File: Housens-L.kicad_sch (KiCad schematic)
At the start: 47 parts, among them J1 JTAG/SWD, J2 USB_C_2.0, Q1 BSS138DWQ, SW1 RESET, SW2 USER, U1 MCP1603, U2 BME280, U3 OPT3005, U4 STM32WB55CGUx, U5 STCC4, U6 REG710NA-3.3, Y1 32MHz, Y2 32.768kHz

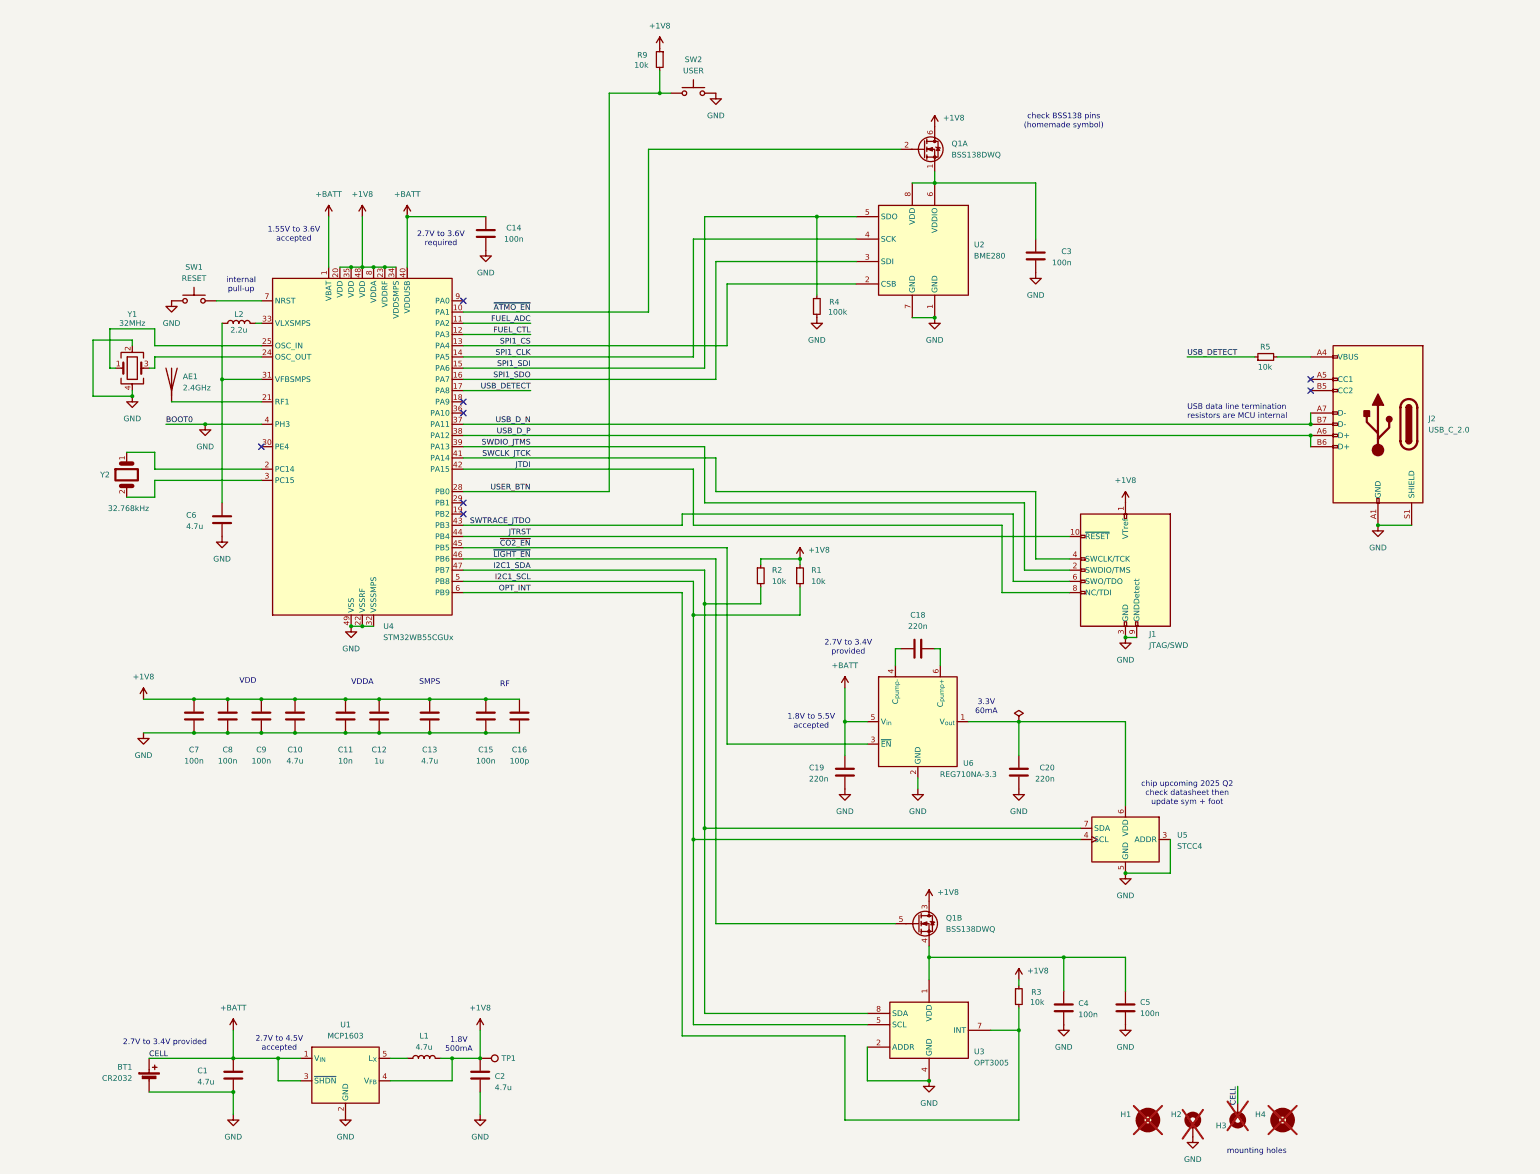
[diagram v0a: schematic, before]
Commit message: Use proper load switch instead of plain FET
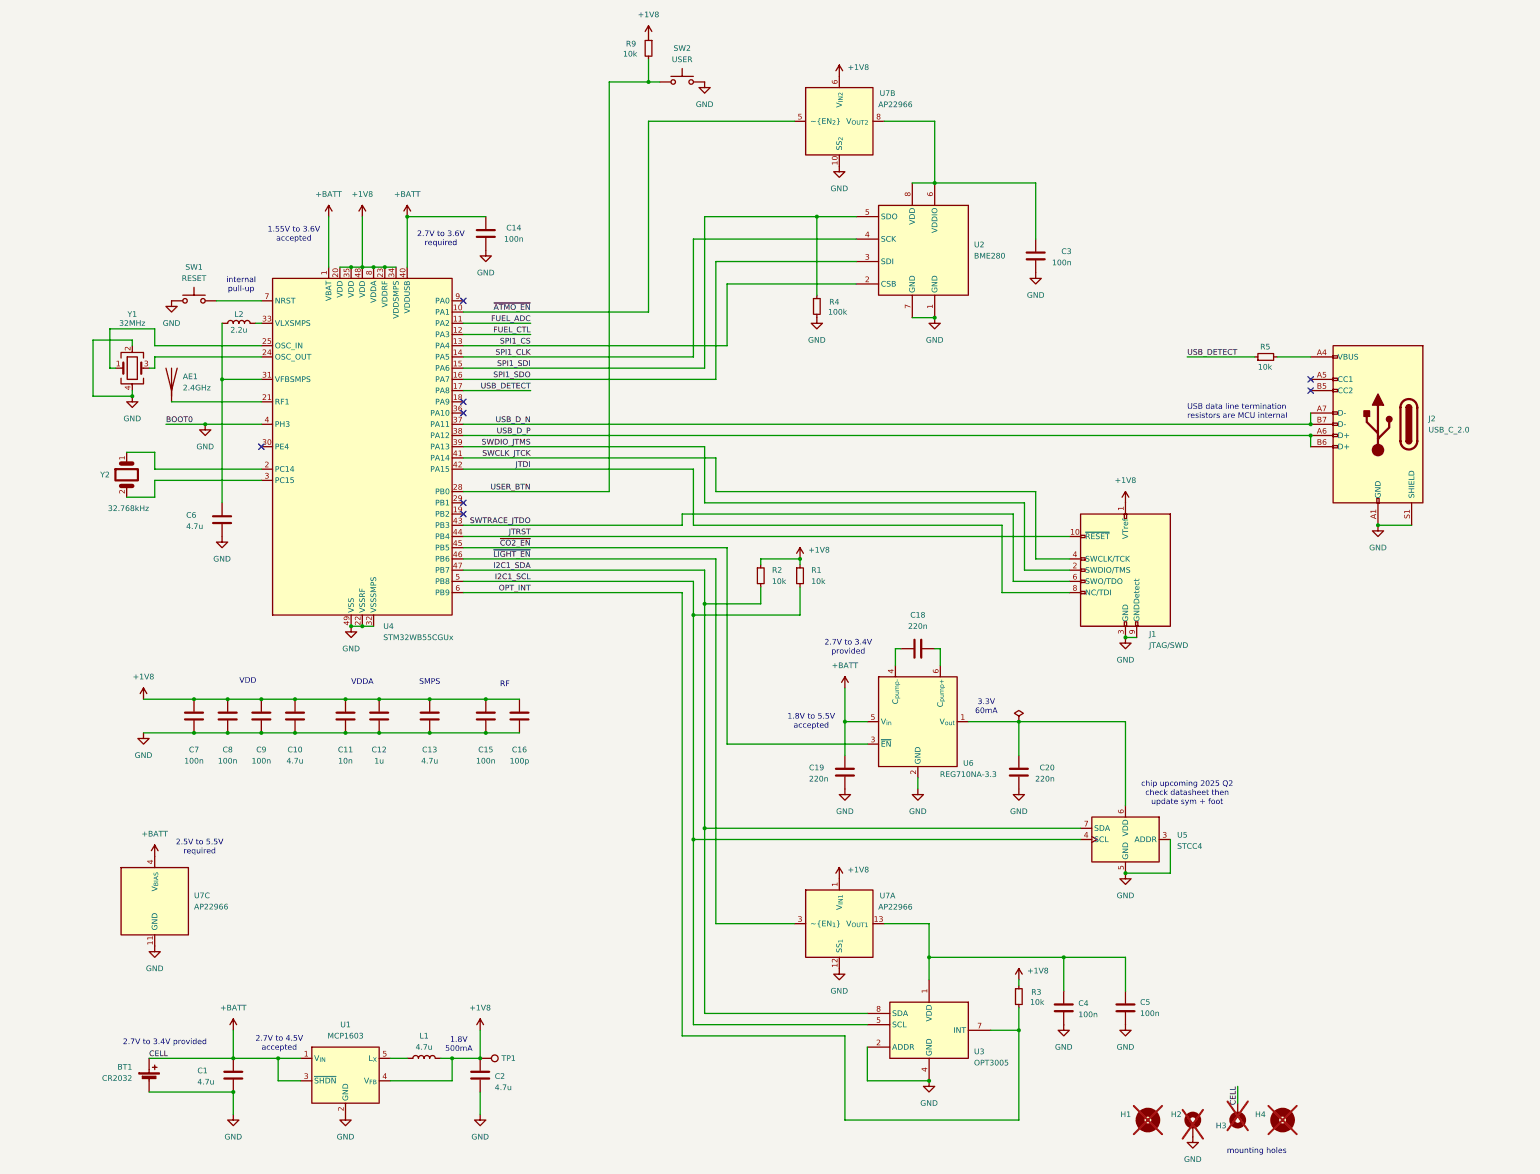
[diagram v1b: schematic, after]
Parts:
- removed Q1: BSS138DWQ, Package_TO_SOT_SMD:SOT-363_SC-70-6, symbol Invented:BSS138DWQ
- added U7: AP22966, Invented:DFN-14-1EP_3x2mm_P0.4mm_EP1.78x1.35mm_AP22966, symbol Invented:AP22966_Split
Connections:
- net +1V8: now also U7.1 (V_{IN1}), U7.2 (V_{IN1}), U7.6 (V_{IN2}), U7.7 (V_{IN2})
- net +BATT: now also U7.4 (V_{BIAS})
- net GND: now also U7.10 (SS_{2}), U7.11 (GND), U7.12 (SS_{1}), U7.15 (GND)
- net ~{ATMO_EN}: now also U7.5 (~{EN_{2}})
- net ~{LIGHT_EN}: now also U7.3 (~{EN_{1}})
- net at C4.1, C5.1, U3.1 (VDD): now also U7.13 (V_{OUT1}), U7.14 (V_{OUT1})
- net at C3.1, U2.6 (VDDIO), U2.8 (VDD): now also U7.8 (V_{OUT2}), U7.9 (V_{OUT2})
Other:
- note added: "2.5V to 5.5V required"
- note removed: "check BSS138 pins (homemade symbol)"
- moved on the sheet: R9, SW2

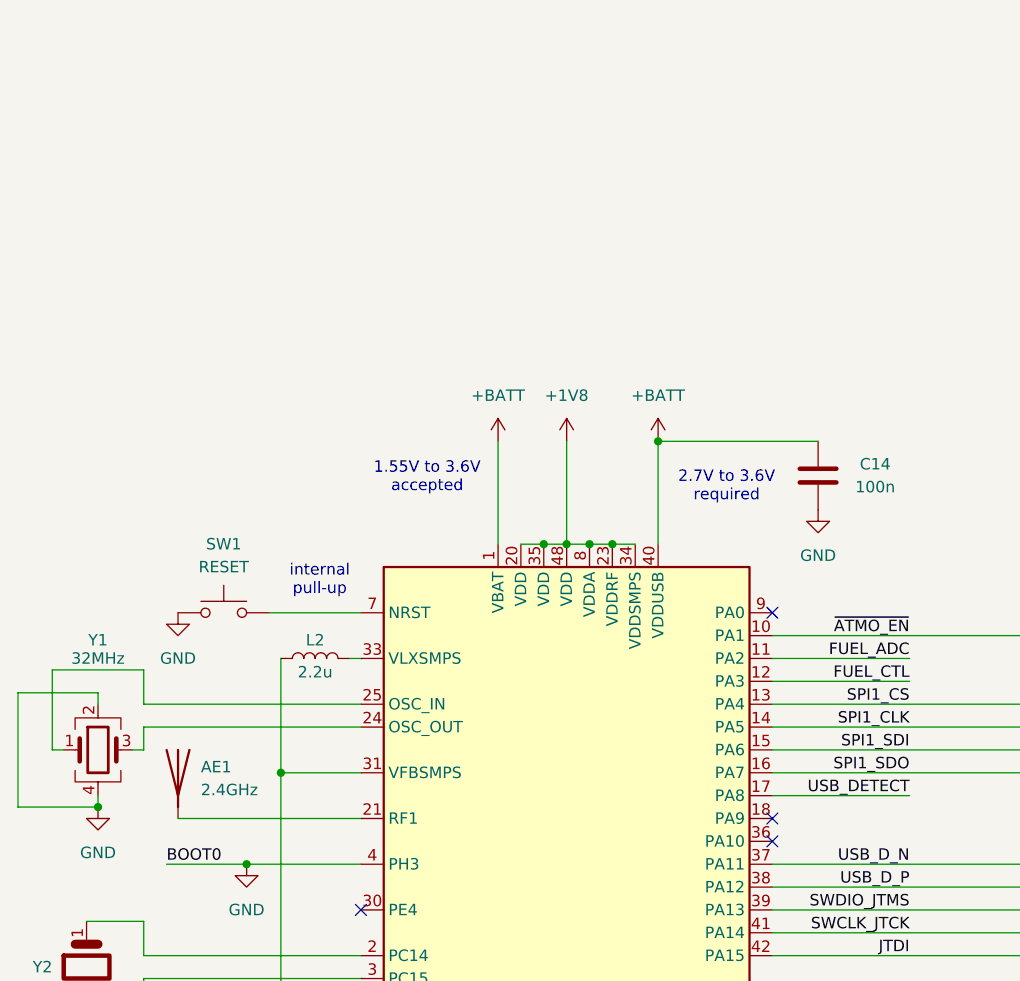
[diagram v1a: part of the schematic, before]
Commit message: Add matching circuit to antenna
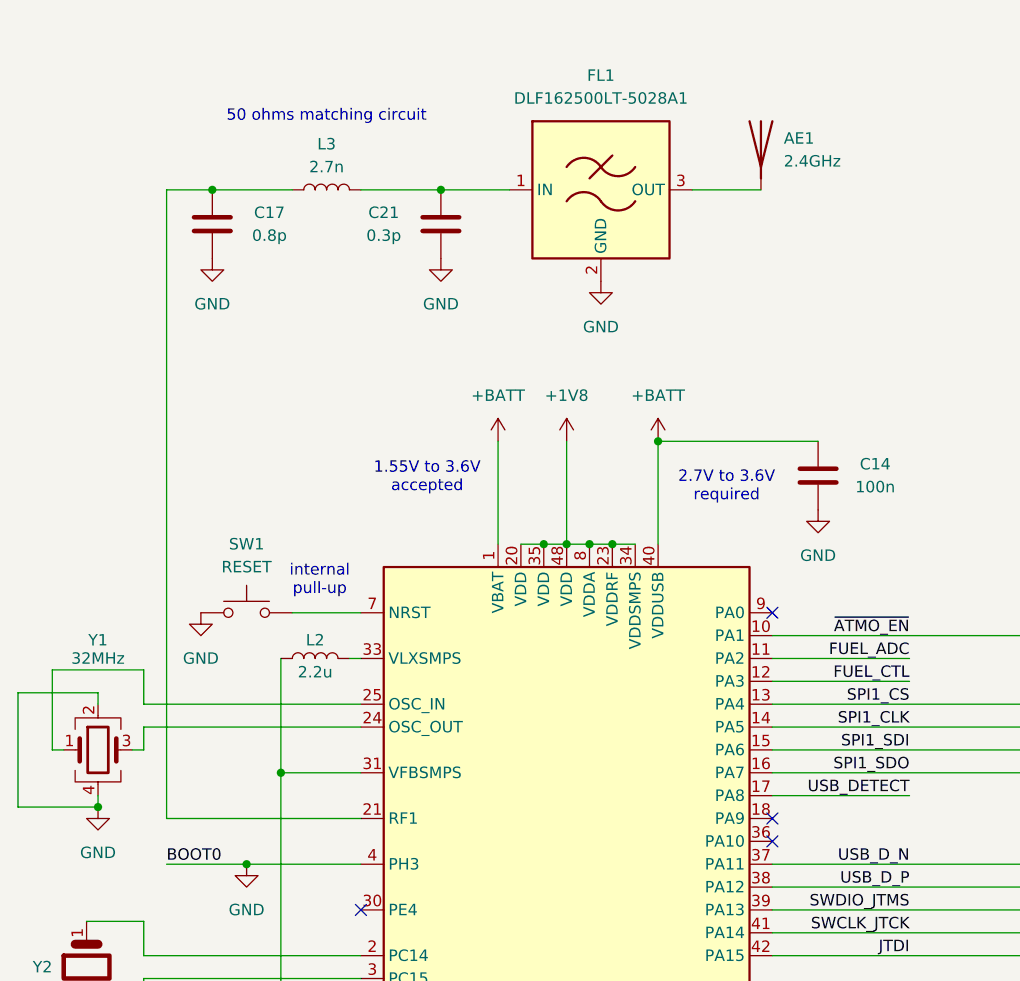
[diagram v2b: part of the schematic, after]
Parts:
- added C17: 0.8p, Capacitor_SMD:C_0603_1608Metric, symbol Device:C
- added C21: 0.3p, Capacitor_SMD:C_0603_1608Metric, symbol Device:C
- added FL1: DLF162500LT-5028A1, Invented:DLF162500LT-5028A1, symbol RF_Filter:LFCN-2400D
- added L3: 2.7n, Inductor_SMD:L_0603_1608Metric, symbol Device:L
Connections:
- net GND: now also C17.1, C21.1, FL1.2 (GND), FL1.4 (GND)
- net at U4.21 (RF1): now also C17.2, L3.1; no longer AE1.1 (A)
- new net: C21.2, FL1.1 (IN), L3.2
- new net: AE1.1 (A), FL1.3 (OUT)
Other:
- note added: "50 ohms matching circuit"
- moved on the sheet: SW1

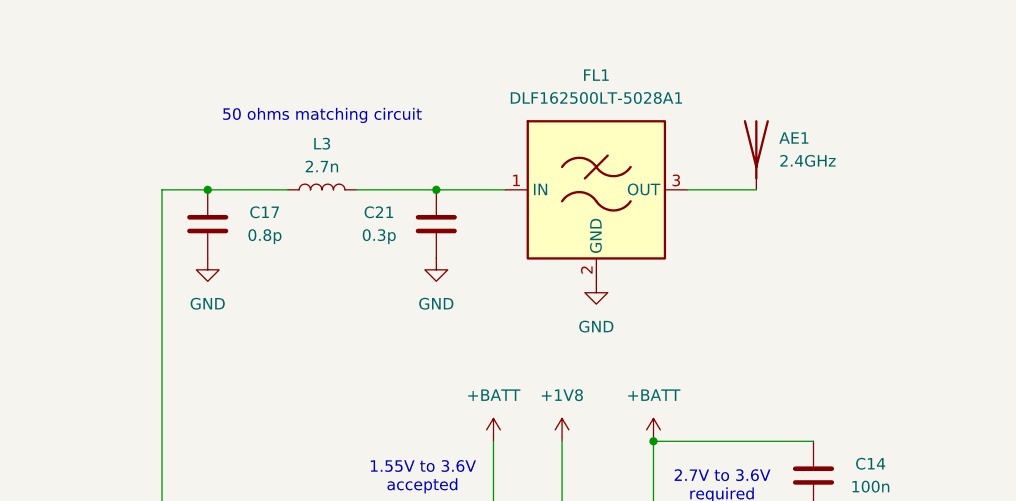
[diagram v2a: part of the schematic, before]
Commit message: Replace matching circuit with IPD
This is more compact, purpose-made, and cheaper than the individual components!
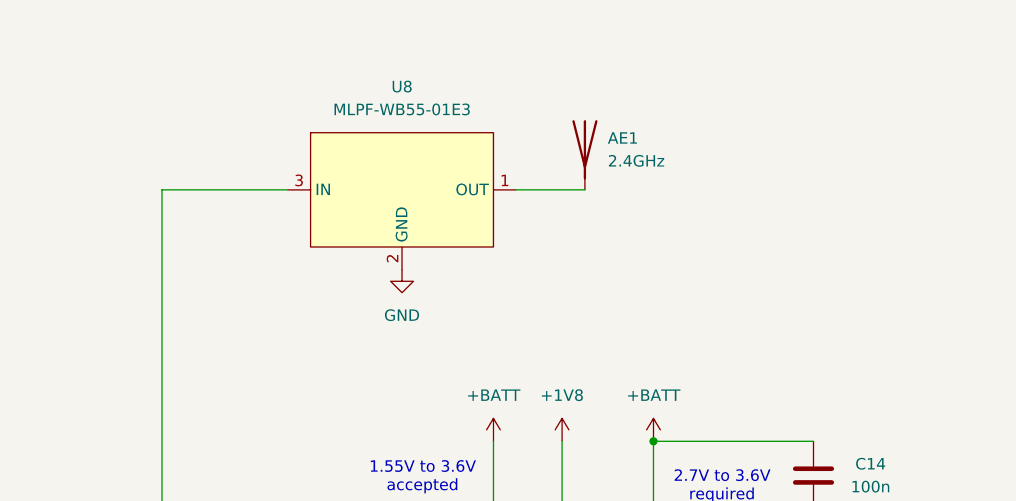
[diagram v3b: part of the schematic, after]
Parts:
- removed C17: 0.8p, Capacitor_SMD:C_0603_1608Metric, symbol Device:C
- removed C21: 0.3p, Capacitor_SMD:C_0603_1608Metric, symbol Device:C
- removed FL1: DLF162500LT-5028A1, Invented:DLF162500LT-5028A1, symbol RF_Filter:LFCN-2400D
- removed L3: 2.7n, Inductor_SMD:L_0603_1608Metric, symbol Device:L
- added U8: MLPF-WB55-01E3, Invented:MLPF-WB55-01E3, symbol Invented:MLPF-WB55-01E3
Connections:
- net GND: now also U8.2 (GND), U8.4 (GND), U8.5 (GND), U8.6 (GND)
- net at U4.21 (RF1): now also U8.3 (IN)
- net at AE1.1 (A): now also U8.1 (OUT)
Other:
- note removed: "50 ohms matching circuit"
- moved on the sheet: AE1
